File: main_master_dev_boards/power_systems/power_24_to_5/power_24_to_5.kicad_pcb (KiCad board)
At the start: 2 copper layers, 67 x 30 mm, 23 parts, among them J1 Switch_in, J2 24_in, J3 GND_in, J4 PGood_out, J5 ref_out, J6 5_out, J7 GND_out, U1 LMR16030

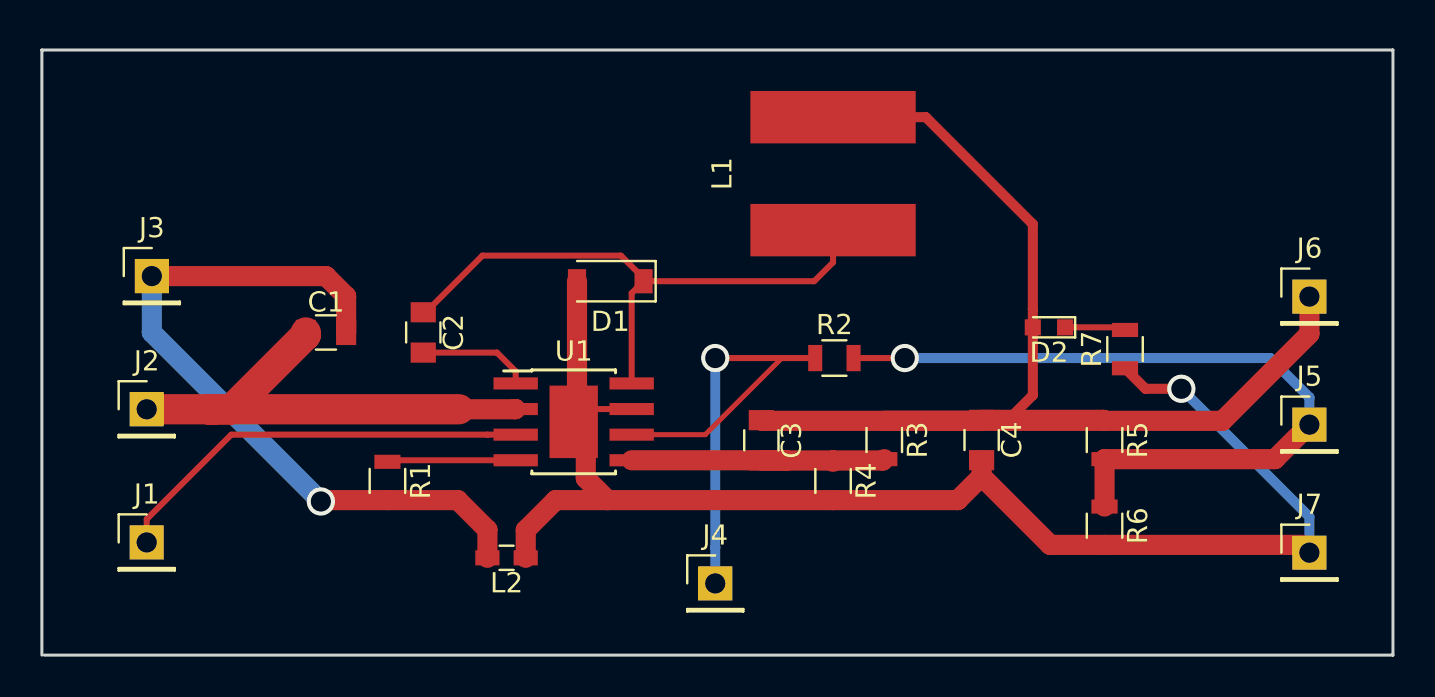
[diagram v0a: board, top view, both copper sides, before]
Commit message: Generated gerber files for 24_to_5 and power_switch dev boards
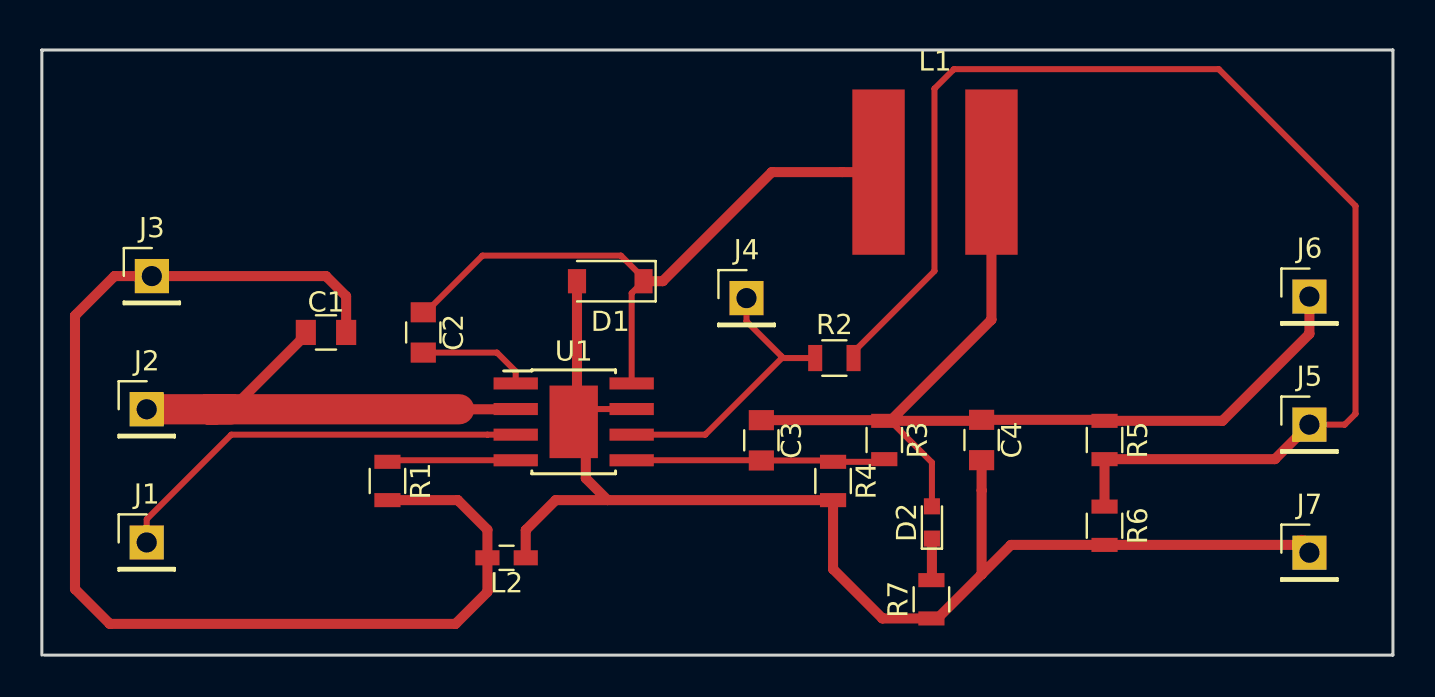
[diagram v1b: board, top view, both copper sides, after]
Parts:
- moved R7 15.7 mm to (115.1, 61.2)
- moved J4 14.2 mm to (105.9, 46.3)
- moved D2 11.3 mm to (115.1, 57.4), turned to 90 degrees
- moved L1 5.06 mm to (115.3, 40.1), turned to 0 degrees
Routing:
- net /P_ref_buc: track 38.0 -> 65.2 mm, vias 1 -> 0
- net /GND24: track 36.8 -> 60.5 mm, vias 1 -> 0
- net /V5_MAIN: track 64.1 -> 50.7 mm
- net /PG_v5_main: track 26.8 -> 14.4 mm, vias 1 -> 0
- net /GND: track 74.8 -> 69.4 mm, vias 1 -> 0
- net Net-(C2-Pad1): track 29.4 -> 31.9 mm
- net Net-(C3-Pad2): track 13.9 -> 12.6 mm
- net Net-(D2-Pad1): track 3.03 -> 2.07 mm

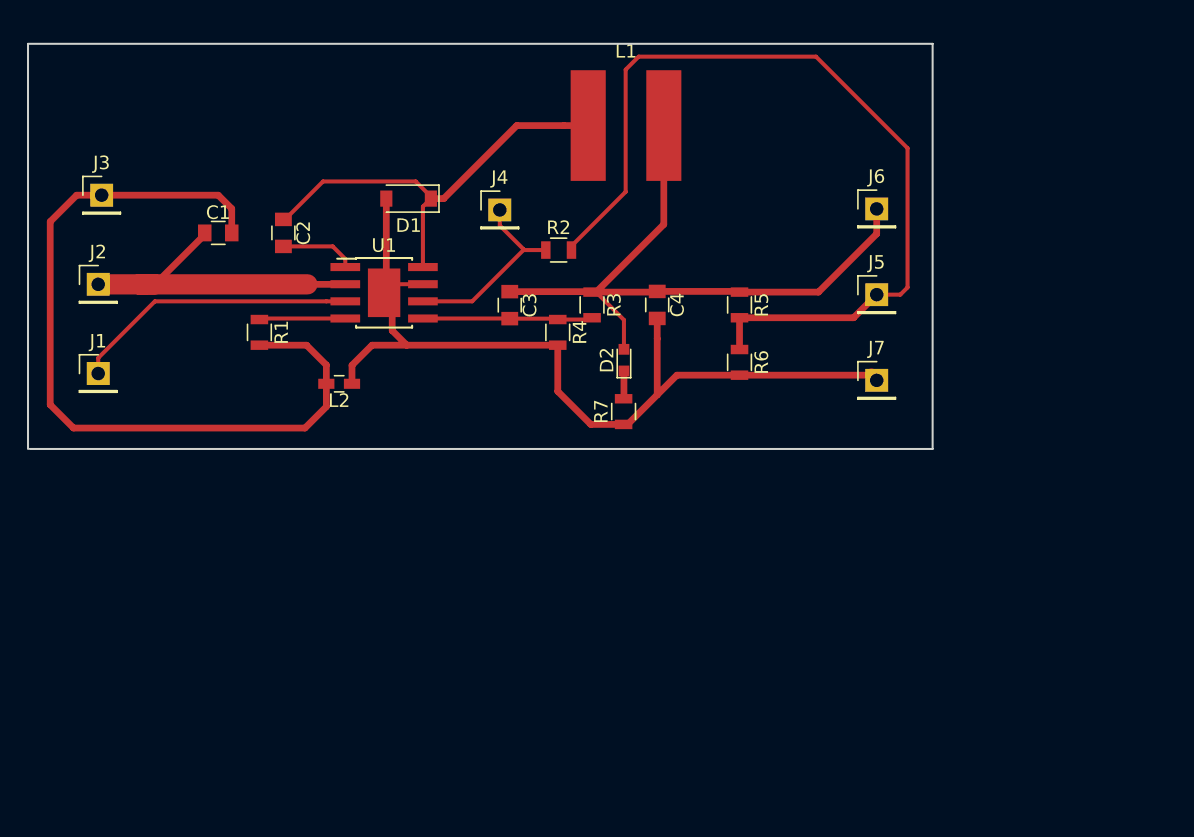
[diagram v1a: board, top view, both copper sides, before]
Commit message: Started Adding 3v3 power LDO to 24_to_5 dev board
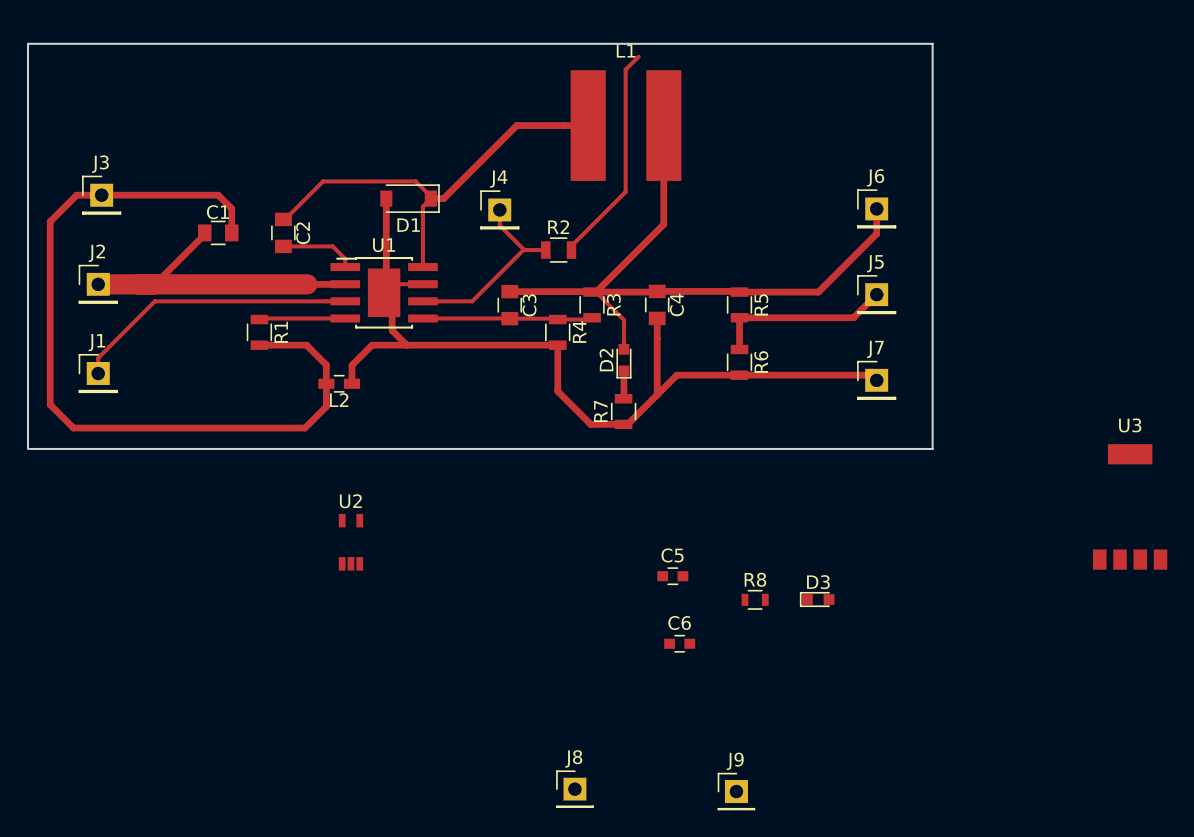
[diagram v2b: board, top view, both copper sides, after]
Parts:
- added C5: 22uF, Capacitors_SMD:C_0603, F.Cu at (118.8, 73.4)
- added C6: 22uF, Capacitors_SMD:C_0603, F.Cu at (119.3, 78.4)
- added D3: GRN_LED, LEDs:LED_0603, F.Cu at (129.5, 75.2)
- added J8: 3v3_out, Pin_Headers:Pin_Header_Straight_1x01_Pitch2.54mm, F.Cu at (111.5, 89.2)
- added J9: PGoodBackup_out, Pin_Headers:Pin_Header_Straight_1x01_Pitch2.54mm, F.Cu at (123.5, 89.4)
- added R8: 10, Resistors_SMD:R_0603, F.Cu at (124.9, 75.2)
- added U2: 74AUC1G32, SO-70:SO-70, F.Cu at (94.9, 70.9)
- added U3: LP3852-3.3, SOT-223:SOT-223, F.Cu at (152.6, 68.3)
- J4: value PGood_out -> PGoodMain_out
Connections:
- net /GND renamed GND
- D2 pad 2: /V5_MAIN -> Net-(D2-Pad2)
- R7 pad 2: Net-(D2-Pad1) -> Net-(R7-Pad2)
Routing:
- net /P_ref_buc: track 65.2 -> 29.6 mm
- net Net-(D2-Pad2): track 0.00 -> 2.18 mm
- net /V5_MAIN: track 50.7 -> 48.5 mm
- net Net-(R7-Pad2): track 0.00 -> 2.07 mm
- net Net-(D2-Pad1): track 2.07 -> 0.00 mm

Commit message: Placed 3v3 LDO and components. Need to route
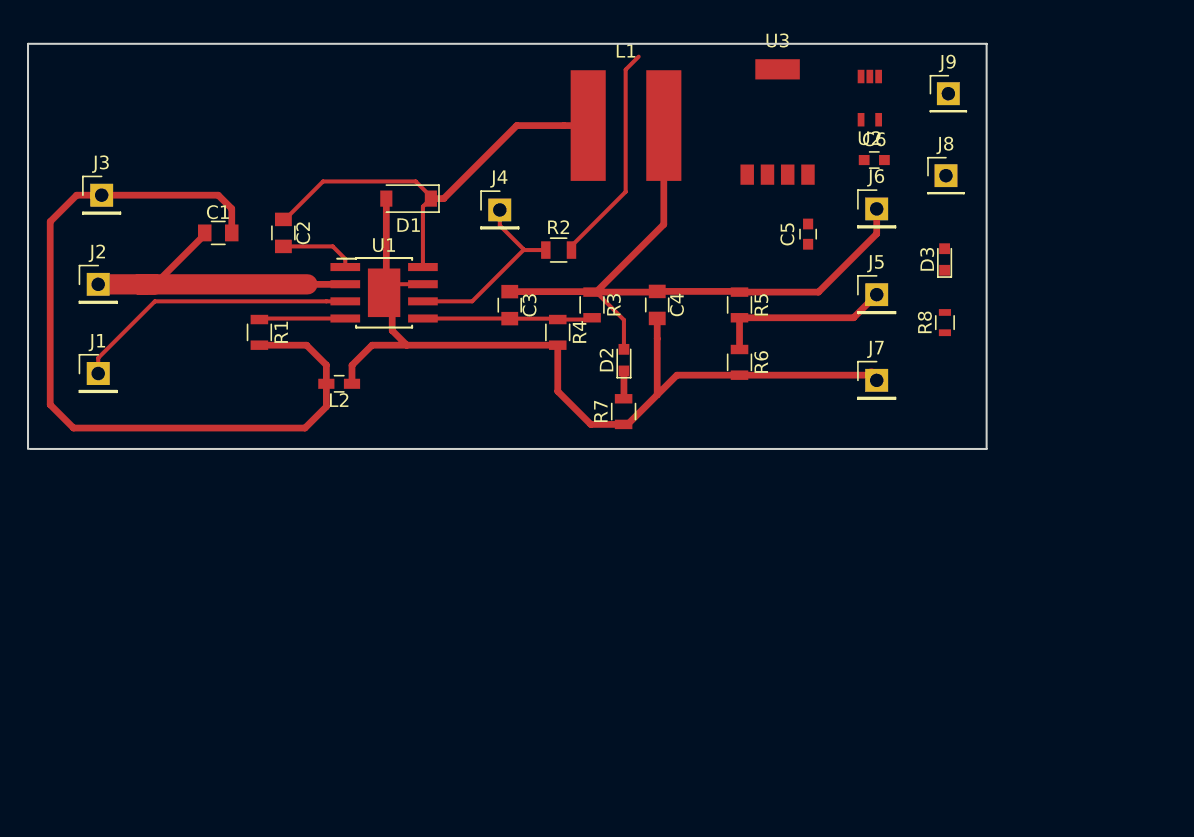
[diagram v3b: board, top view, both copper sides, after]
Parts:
- moved J9 54.0 mm to (139.2, 37.7)
- moved J8 53.1 mm to (139.0, 43.8)
- moved U2 50.6 mm to (133.3, 38.0), turned to 180 degrees
- moved U3 38.7 mm to (126.5, 39.8)
- moved C6 38.6 mm to (133.7, 42.6)
- moved C5 27.2 mm to (128.8, 48.1), turned to 90 degrees
- moved D3 26.9 mm to (138.9, 50.0), turned to 90 degrees
- moved R8 24.9 mm to (138.9, 54.6), turned to 90 degrees
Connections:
- D3 pad 2: /3V3 -> /3V3_out
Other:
- board size 67 x 30 mm -> 71 x 30 mm
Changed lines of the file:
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@@
 (kicad_pcb (version 4) (host pcbnew 4.0.4-stable)
   (general
-    (links 49)
-    (no_connects 12)
-    (area 70.924999 33.924999 138.075001 64.083001)
+    (links 50)
+    (no_connects 16)
+    (area 70.924999 33.924999 142.075001 64.083001)
     (thickness 1.6)
     (drawings 4)
@@
     (zones 0)
     (modules 31)
-    (nets 21)
+    (nets 20)
   )
   (page A4)
@@
   (net 13 /3V3_out)
   (net 14 "Net-(D2-Pad2)")
-  (net 15 /3V3)
-  (net 16 "Net-(D3-Pad1)")
-  (net 17 /PG_v5_backup)
-  (net 18 "Net-(R7-Pad2)")
-  (net 19 VCC)
-  (net 20 /v5_good)
+  (net 15 "Net-(D3-Pad1)")
+  (net 16 /PG_v5_backup)
+  (net 17 "Net-(R7-Pad2)")
+  (net 18 VCC)
+  (net 19 /v5_good)
   (net_class Default "This is the default net class."
     (clearance 0.25)
@@
     (uvia_dia 0.3)
     (uvia_drill 0.1)
-    (add_net /3V3)
     (add_net /3V3_out)
     (add_net /GND24)
@@
       (net 12 GND))
     (pad 2 smd rect (at 0.95 0 90) (size 0.7 1.3) (layers F.Cu F.Paste F.Mask)
-      (net 18 "Net-(R7-Pad2)"))
+      (net 17 "Net-(R7-Pad2)"))
     (model Resistors_SMD.3dshapes/R_0805.wrl
       (at (xyz 0 0 0))
@@
   )
   (module Capacitors_SMD:C_0603 (layer F.Cu)
-    (at 118.757 73.4314)
+    (at 128.778 48.0956 90)
     (descr "Capacitor SMD 0603, reflow soldering, AVX (see smccp.pdf)")
     (tags "capacitor 0603")
     (attr smd)
-    (fp_text reference C5 (at 0 -1.5) (layer F.SilkS)
-      (effects (font (size 1 1) (thickness 0.15)))
-    )
-    (fp_text value 22uF (at 0 1.5) (layer F.Fab)
-      (effects (font (size 1 1) (thickness 0.15)))
-    )
-    (fp_text user %R (at 0 -1.5) (layer F.Fab)
+    (fp_text reference C5 (at 0 -1.5 90) (layer F.SilkS)
+      (effects (font (size 1 1) (thickness 0.15)))
+    )
+    (fp_text value 22uF (at 0 1.5 90) (layer F.Fab)
+      (effects (font (size 1 1) (thickness 0.15)))
+    )
+    (fp_text user %R (at 0 -1.5 90) (layer F.Fab)
       (effects (font (size 1 1) (thickness 0.15)))
     )
@@
     (fp_line (start 1.4 0.65) (end 1.4 -0.65) (layer F.CrtYd) (width 0.05))
     (fp_line (start 1.4 0.65) (end -1.4 0.65) (layer F.CrtYd) (width 0.05))
-    (pad 1 smd rect (at -0.75 0) (size 0.8 0.75) (layers F.Cu F.Paste F.Mask)
+    (pad 1 smd rect (at -0.75 0 90) (size 0.8 0.75) (layers F.Cu F.Paste F.Mask)
       (net 5 /V5_MAIN))
-    (pad 2 smd rect (at 0.75 0) (size 0.8 0.75) (layers F.Cu F.Paste F.Mask)
+    (pad 2 smd rect (at 0.75 0 90) (size 0.8 0.75) (layers F.Cu F.Paste F.Mask)
       (net 12 GND))
     (model Capacitors_SMD.3dshapes/C_0603.wrl
@@
   )
   (module Capacitors_SMD:C_0603 (layer F.Cu)
-    (at 119.2664 78.4352)
+    (at 133.6802 42.6085)
     (descr "Capacitor SMD 0603, reflow soldering, AVX (see smccp.pdf)")
     (tags "capacitor 0603")
@@
   )
   (module LEDs:LED_0603 (layer F.Cu)
-    (at 129.5274 75.1586)
+    (at 138.8872 49.9744 90)
     (descr "LED 0603 smd package")
     (tags "LED led 0603 SMD smd SMT smt smdled SMDLED smtled SMTLED")
     (attr smd)
-    (fp_text reference D3 (at 0 -1.25) (layer F.SilkS)
-      (effects (font (size 1 1) (thickness 0.15)))
-    )
-    (fp_text value GRN_LED (at 0 1.35) (layer F.Fab)
+    (fp_text reference D3 (at 0 -1.25 90) (layer F.SilkS)
+      (effects (font (size 1 1) (thickness 0.15)))
+    )
+    (fp_text value GRN_LED (at 0 1.35 90) (layer F.Fab)
       (effects (font (size 1 1) (thickness 0.15)))
     )
@@
     (fp_line (start -1.45 0.65) (end -1.45 -0.65) (layer F.CrtYd) (width 0.05))
     (fp_line (start -1.45 -0.65) (end 1.45 -0.65) (layer F.CrtYd) (width 0.05))
-    (pad 2 smd rect (at 0.8 0 180) (size 0.8 0.8) (layers F.Cu F.Paste F.Mask)
-      (net 15 /3V3))
-    (pad 1 smd rect (at -0.8 0 180) (size 0.8 0.8) (layers F.Cu F.Paste F.Mask)
-      (net 16 "Net-(D3-Pad1)"))
+    (pad 2 smd rect (at 0.8 0 270) (size 0.8 0.8) (layers F.Cu F.Paste F.Mask)
+      (net 13 /3V3_out))
+    (pad 1 smd rect (at -0.8 0 270) (size 0.8 0.8) (layers F.Cu F.Paste F.Mask)
+      (net 15 "Net-(D3-Pad1)"))
     (model LEDs.3dshapes/LED_0603.wrl
       (at (xyz 0 0 0))
@@
   )
   (module Pin_Headers:Pin_Header_Straight_1x01_Pitch2.54mm (layer F.Cu)
-    (at 111.506 89.2048)
+    (at 138.9888 43.7642)
     (descr "Through hole straight pin header, 1x01, 2.54mm pitch, single row")
     (tags "Through hole pin header THT 1x01 2.54mm single row")
@@
   )
   (module Pin_Headers:Pin_Header_Straight_1x01_Pitch2.54mm (layer F.Cu)
-    (at 123.4694 89.3826)
+    (at 139.1666 37.6936)
     (descr "Through hole straight pin header, 1x01, 2.54mm pitch, single row")
     (tags "Through hole pin header THT 1x01 2.54mm single row")
@@
     )
     (pad 1 thru_hole rect (at 0 0) (size 1.7 1.7) (drill 1) (layers *.Cu *.Mask)
-      (net 17 /PG_v5_backup))
+      (net 16 /PG_v5_backup))
     (model ${KISYS3DMOD}/Pin_Headers.3dshapes/Pin_Header_Straight_1x01_Pitch2.54mm.wrl
       (at (xyz 0 0 0))
@@
   )
   (module Resistors_SMD:R_0603 (layer F.Cu)
-    (at 124.853 75.184)
+    (at 138.9126 54.6488 90)
     (descr "Resistor SMD 0603, reflow soldering, Vishay (see dcrcw.pdf)")
     (tags "resistor 0603")
     (attr smd)
-    (fp_text reference R8 (at 0 -1.45) (layer F.SilkS)
-      (effects (font (size 1 1) (thickness 0.15)))
-    )
-    (fp_text value 10 (at 0 1.5) (layer F.Fab)
-      (effects (font (size 1 1) (thickness 0.15)))
-    )
-    (fp_text user %R (at 0 0) (layer F.Fab)
+    (fp_text reference R8 (at 0 -1.45 90) (layer F.SilkS)
+      (effects (font (size 1 1) (thickness 0.15)))
+    )
+    (fp_text value 10 (at 0 1.5 90) (layer F.Fab)
+      (effects (font (size 1 1) (thickness 0.15)))
+    )
+    (fp_text user %R (at 0 0 90) (layer F.Fab)
       (effects (font (size 0.5 0.5) (thickness 0.075)))
     )
@@
     (fp_line (start 1.25 0.7) (end 1.25 -0.7) (layer F.CrtYd) (width 0.05))
     (fp_line (start 1.25 0.7) (end -1.25 0.7) (layer F.CrtYd) (width 0.05))
-    (pad 1 smd rect (at -0.75 0) (size 0.5 0.9) (layers F.Cu F.Paste F.Mask)
-      (net 12 GND))
-    (pad 2 smd rect (at 0.75 0) (size 0.5 0.9) (layers F.Cu F.Paste F.Mask)
-      (net 16 "Net-(D3-Pad1)"))
+    (pad 1 smd rect (at -0.75 0 90) (size 0.5 0.9) (layers F.Cu F.Paste F.Mask)
+      (net 12 GND))
+    (pad 2 smd rect (at 0.75 0 90) (size 0.5 0.9) (layers F.Cu F.Paste F.Mask)
+      (net 15 "Net-(D3-Pad1)"))
     (model ${KISYS3DMOD}/Resistors_SMD.3dshapes/R_0603.wrl
       (at (xyz 0 0 0))
@@
   )
   (module SO-70:SO-70 (layer F.Cu)
-    (at 94.9198 70.9168)
-    (fp_text reference U2 (at 0 -3) (layer F.SilkS)
-      (effects (font (size 1 1) (thickness 0.15)))
-    )
-    (fp_text value 74AUC1G32 (at 0 3) (layer F.Fab)
-      (effects (font (size 1 1) (thickness 0.15)))
-    )
-    (pad 1 smd rect (at -0.65 1.6) (size 0.5 1) (layers F.Cu F.Paste F.Mask)
+    (at 133.35 38.0238 180)
+    (fp_text reference U2 (at 0 -3 180) (layer F.SilkS)
+      (effects (font (size 1 1) (thickness 0.15)))
+    )
+    (fp_text value 74AUC1G32 (at 0 3 180) (layer F.Fab)
+      (effects (font (size 1 1) (thickness 0.15)))
+    )
+    (pad 1 smd rect (at -0.65 1.6 180) (size 0.5 1) (layers F.Cu F.Paste F.Mask)
       (net 9 /PG_v5_main))
-    (pad 2 smd rect (at 0 1.6) (size 0.5 1) (layers F.Cu F.Paste F.Mask)
-      (net 17 /PG_v5_backup))
-    (pad 3 smd rect (at 0.65 1.6) (size 0.5 1) (layers F.Cu F.Paste F.Mask)
-      (net 12 GND))
-    (pad 5 smd rect (at -0.65 -1.6) (size 0.5 1) (layers F.Cu F.Paste F.Mask)
-      (net 19 VCC))
-    (pad 4 smd rect (at 0.65 -1.6) (size 0.5 1) (layers F.Cu F.Paste F.Mask)
-      (net 20 /v5_good))
+    (pad 2 smd rect (at 0 1.6 180) (size 0.5 1) (layers F.Cu F.Paste F.Mask)
+      (net 16 /PG_v5_backup))
+    (pad 3 smd rect (at 0.65 1.6 180) (size 0.5 1) (layers F.Cu F.Paste F.Mask)
+      (net 12 GND))
+    (pad 5 smd rect (at -0.65 -1.6 180) (size 0.5 1) (layers F.Cu F.Paste F.Mask)
+      (net 18 VCC))
+    (pad 4 smd rect (at 0.65 -1.6 180) (size 0.5 1) (layers F.Cu F.Paste F.Mask)
+      (net 19 /v5_good))
   )
   (module SOT-223:SOT-223 (layer F.Cu)
-    (at 152.6286 68.3006)
+    (at 126.5174 39.7902)
     (fp_text reference U3 (at 0 -6) (layer F.SilkS)
       (effects (font (size 1 1) (thickness 0.15)))
@@
     )
     (pad 1 smd rect (at -2.25 3.9) (size 1 1.5) (layers F.Cu F.Paste F.Mask)
-      (net 20 /v5_good))
+      (net 19 /v5_good))
     (pad 2 smd rect (at -0.75 3.9) (size 1 1.5) (layers F.Cu F.Paste F.Mask)
       (net 5 /V5_MAIN))
@@
   )
   (gr_line (start 71 64.008) (end 71 34) (layer Edge.Cuts) (width 0.15))
-  (gr_line (start 138 64.008) (end 71.12 64.008) (layer Edge.Cuts) (width 0.15))
-  (gr_line (start 138 34) (end 138 64.008) (layer Edge.Cuts) (width 0.15))
-  (gr_line (start 71 34) (end 138 34) (layer Edge.Cuts) (width 0.15))
+  (gr_line (start 142 64.008) (end 71.12 64.008) (layer Edge.Cuts) (width 0.15))
+  (gr_line (start 142 34) (end 142 64.008) (layer Edge.Cuts) (width 0.15))
+  (gr_line (start 71 34) (end 142 34) (layer Edge.Cuts) (width 0.15))
   (segment (start 76.2 51.816) (end 79.248 51.816) (width 1.5) (layer F.Cu) (net 1))
   (segment (start 84.09 48.131) (end 80.405 51.816) (width 0.5) (layer F.Cu) (net 1))
@@
   (segment (start 96.873999 51.805) (end 96.774 51.705001) (width 0.3) (layer F.Cu) (net 12))
   (segment (start 115.1382 56.6294) (end 115.1382 54.4522) (width 0.3) (layer F.Cu) (net 14))
-  (segment (start 115.1382 58.2294) (end 115.1382 60.264) (width 0.5) (layer F.Cu) (net 18))
-  (segment (start 115.1382 60.264) (end 115.1128 60.2894) (width 0.5) (layer F.Cu) (net 18))
+  (segment (start 115.1382 58.2294) (end 115.1382 60.264) (width 0.5) (layer F.Cu) (net 17))
+  (segment (start 115.1382 60.264) (end 115.1128 60.2894) (width 0.5) (layer F.Cu) (net 17))
 )
